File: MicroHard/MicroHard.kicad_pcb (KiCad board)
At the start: 4 copper layers, 222 x 144.5 mm, 206 parts, among them IC1 IS66WVO32M8DBLL-166BLI, J1 USB_B_Micro, J2 Micro_SD_Card_Det2, J3 GPIO_header, J4 MCU_Debug, J5 Controller Connector, J6 FPGA_GPIO_header, J7 FPGA_DEBUG, J8 L77HDE15SD1CH4FVGA, SW1 KMR221NGLFS, SW2 KMR221NGLFS, SW3 KMR221NGLFS, SW4 KMR221NGLFS, U1 TPS54325, U2 TPS54294, U3 EFM32GG842F1024, U4 XC7A100T-FTG256, U5 MAX6955 Display Driver, U6 SN74ALVC245PWR, U7 SN74ALVC245PWR, U8 MT25QL256ABA8ESF-0SIT, Y1 48MHz, Y2 CB3-3C-20M000000

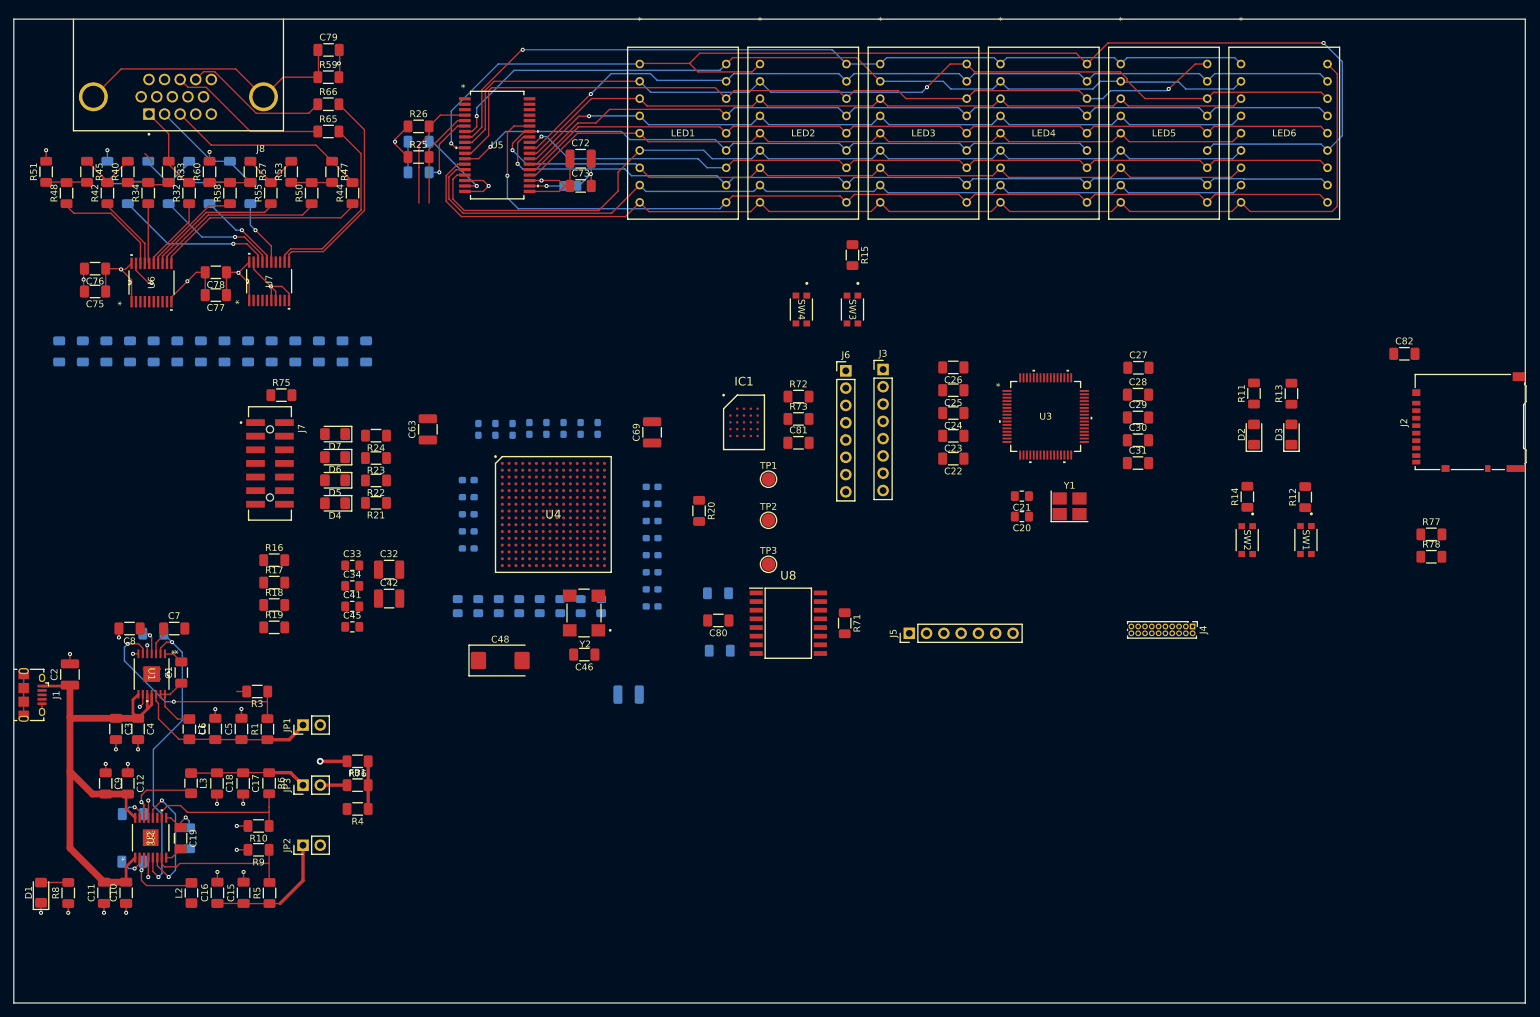
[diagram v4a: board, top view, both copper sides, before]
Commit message: Add MCU
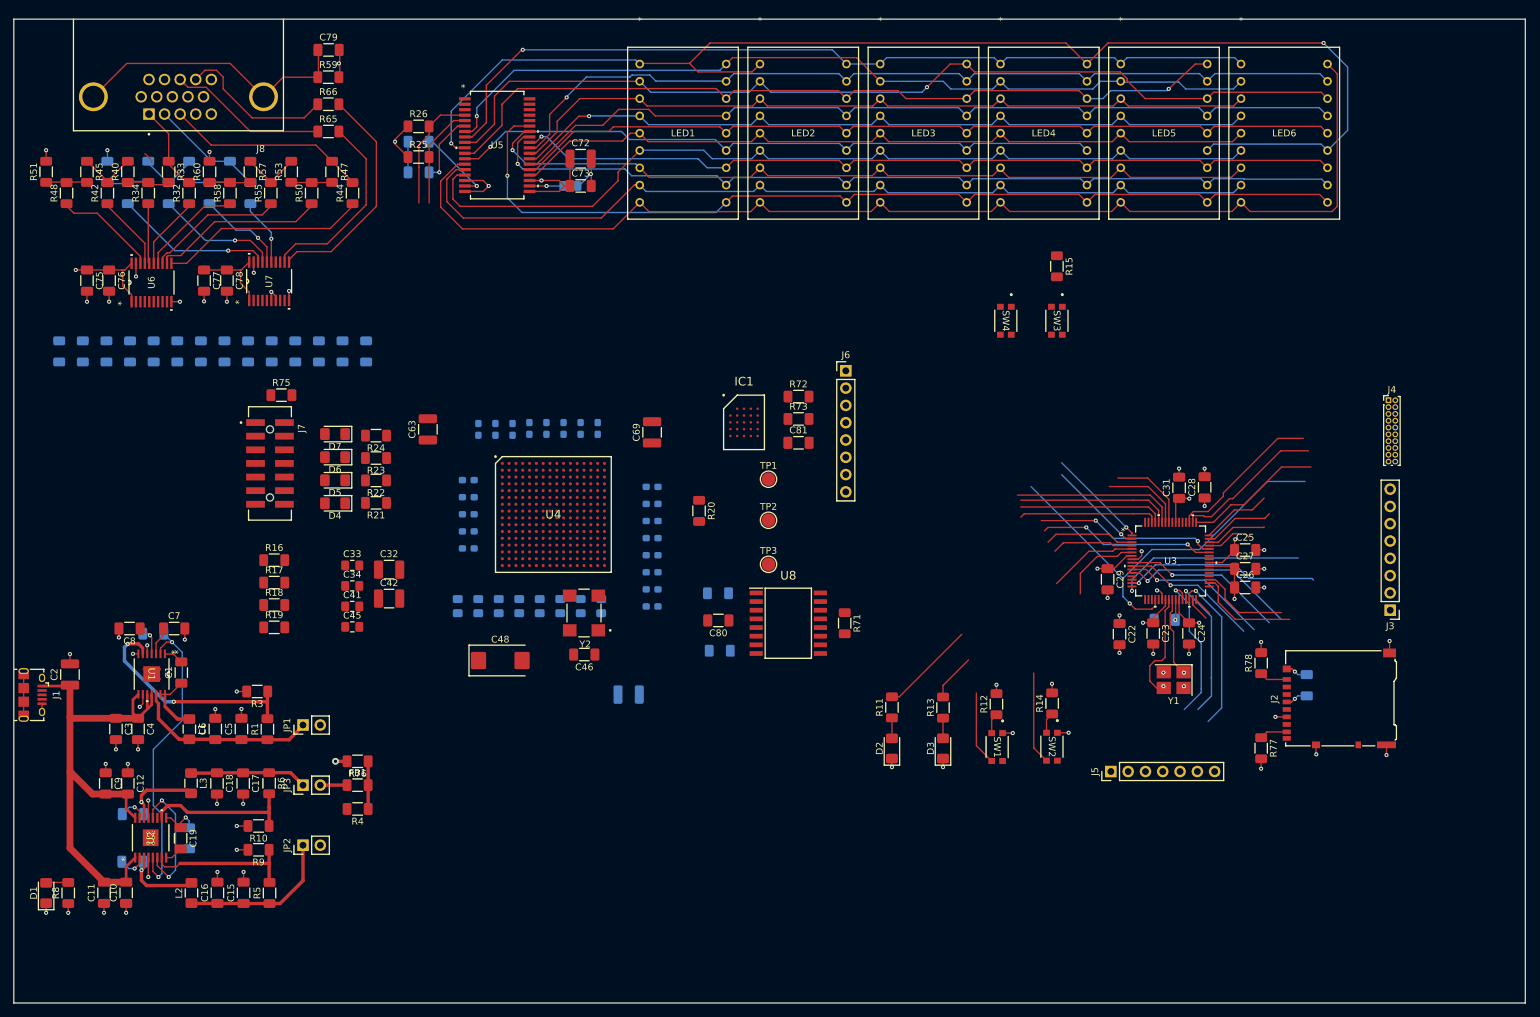
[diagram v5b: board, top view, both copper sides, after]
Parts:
- C20, C21, C30, C82: moved to B.Cu
- moved J3 82.4 mm to (240.2, 115.8), turned to 180 degrees
- moved D2 70.4 mm to (167.0, 136.1)
- moved R11 70.4 mm to (167.0, 130.1)
- moved D3 68.9 mm to (174.5, 136.1)
- moved R13 68.9 mm to (174.5, 130.1)
- moved SW1 54.6 mm to (182.4, 135.9)
- moved R12 54.6 mm to (182.3, 129.6)
- moved C26 53.7 mm to (218.9, 112.5), turned to 0 degrees
- moved C82 50.7 mm to (227.9, 126.8), turned to 90 degrees
- moved C25 48.9 mm to (218.9, 107.0), turned to 0 degrees
- moved C24 47.4 mm to (210.6, 119.2), turned to -90 degrees
- moved J2 44.8 mm to (232.7, 128.8)
- moved J4 43.9 mm to (239.9, 85.0), turned to 0 degrees
- moved SW2 41.8 mm to (190.5, 135.9)
- moved R14 41.8 mm to (190.5, 129.5)
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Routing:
- net MCU_Reset: track 0.00 -> 61.0 mm, vias 0 -> 1
- net +3.3V: track 52.7 -> 97.0 mm, vias 6 -> 18
- net US1_CLK: track 0.00 -> 28.9 mm, vias 0 -> 1
- net US1_CS: track 0.00 -> 28.0 mm, vias 0 -> 1
- net Net-(U3B-PA2): track 0.00 -> 27.3 mm
- net FPGA_RESET: track 0.00 -> 26.6 mm, vias 0 -> 2
- net SD_US2_CS: track 0.00 -> 26.1 mm, vias 0 -> 1
- net FPGA_DONE: track 0.00 -> 25.9 mm, vias 0 -> 2
- net MCU_Btn_2: track 0.00 -> 25.5 mm
- net FPGA_US0_TX: track 0.00 -> 24.2 mm
- net MCU_Btn_1: track 0.00 -> 24.1 mm
- net SD_US2_TX: track 0.00 -> 23.8 mm, vias 0 -> 1
- net Controller_Z: track 0.00 -> 23.6 mm, vias 0 -> 1
- net Net-(J4-Pin_13): track 0.00 -> 22.7 mm
- net FPGA_US0_RX: track 0.00 -> 22.6 mm
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
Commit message: finished memory
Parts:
- removed C58: 470n, Capacitor_SMD:C_0603_1608Metric_Pad1.08x0.95mm_HandSolder
- removed R28, R29, R30, R31, R36, R37, R38, R39, R61, R62, R63, R64, R67, R68: 100k, Resistor_SMD:R_1206_3216Metric_Pad1.30x1.75mm_HandSolder
- C33, C34, C41, C45: moved to B.Cu
- C47, R69, R70: moved to F.Cu
- moved D4 66.8 mm to (148.5, 78.8)
- moved D5 66.8 mm to (148.5, 75.4)
- moved D6 66.8 mm to (148.5, 72.0)
- moved D7 66.8 mm to (148.5, 68.6)
- moved R21 66.8 mm to (154.5, 78.7)
- moved R22 66.8 mm to (154.5, 75.4)
- moved R23 66.8 mm to (154.5, 72.1)
- moved R24 66.8 mm to (154.5, 68.8)
- moved C41 42.8 mm to (125.5, 95.2), turned to -90 degrees
- moved C34 40.6 mm to (126.4, 100.0)
- moved C33 40.1 mm to (127.5, 103.8)
- moved C45 37.0 mm to (123.8, 110.0)
- moved C42 35.9 mm to (117.2, 87.5), turned to 90 degrees
- moved R72 33.0 mm to (121.2, 76.2), turned to 90 degrees
- moved C69 32.2 mm to (102.8, 103.6), turned to 180 degrees
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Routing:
- net GND: track 128.9 -> 226.9 mm, vias 62 -> 131
- net +3.3V: track 97.0 -> 164.6 mm, vias 18 -> 44
- net FPGA_CONFIG_CLOCK: track 0.00 -> 33.4 mm, vias 0 -> 2
- net /FPGA/Unit A/Flash Memory/FLASH_W#: track 0.00 -> 30.8 mm, vias 0 -> 2
- net SRAM_DQ2: track 0.00 -> 28.7 mm, vias 0 -> 2
- net /FPGA/Unit A/Flash Memory/FLASH_HOLD#: track 0.00 -> 26.8 mm
- net +1V0: track 0.00 -> 26.5 mm, vias 0 -> 17
- net SRAM_RESET#: track 0.00 -> 26.2 mm, vias 0 -> 2
- net SRAM_CS#: track 0.00 -> 24.6 mm, vias 0 -> 2
- net /FPGA/Unit A/Flash Memory/FLASH_CS#: track 0.00 -> 22.7 mm, vias 0 -> 2
- net SRAM_DQSM: track 0.00 -> 20.3 mm, vias 0 -> 2
- net SRAM_SCLK: track 0.00 -> 19.8 mm, vias 0 -> 2
- net SRAM_DQ1: track 0.00 -> 19.6 mm, vias 0 -> 2
- net SRAM_DQ5: track 0.00 -> 19.5 mm, vias 0 -> 2
- net /FPGA/Unit A/Flash Memory/FLASH_DQ1: track 0.00 -> 17.6 mm, vias 0 -> 2
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- added copper zone on In4.Cu, net +1V0
- added copper zone on In3.Cu, net +3.3V
- removed copper zone on In2.Cu, net +1V0
- removed copper zone on In2.Cu, net +3.3V
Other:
- copper layers 4 -> 6

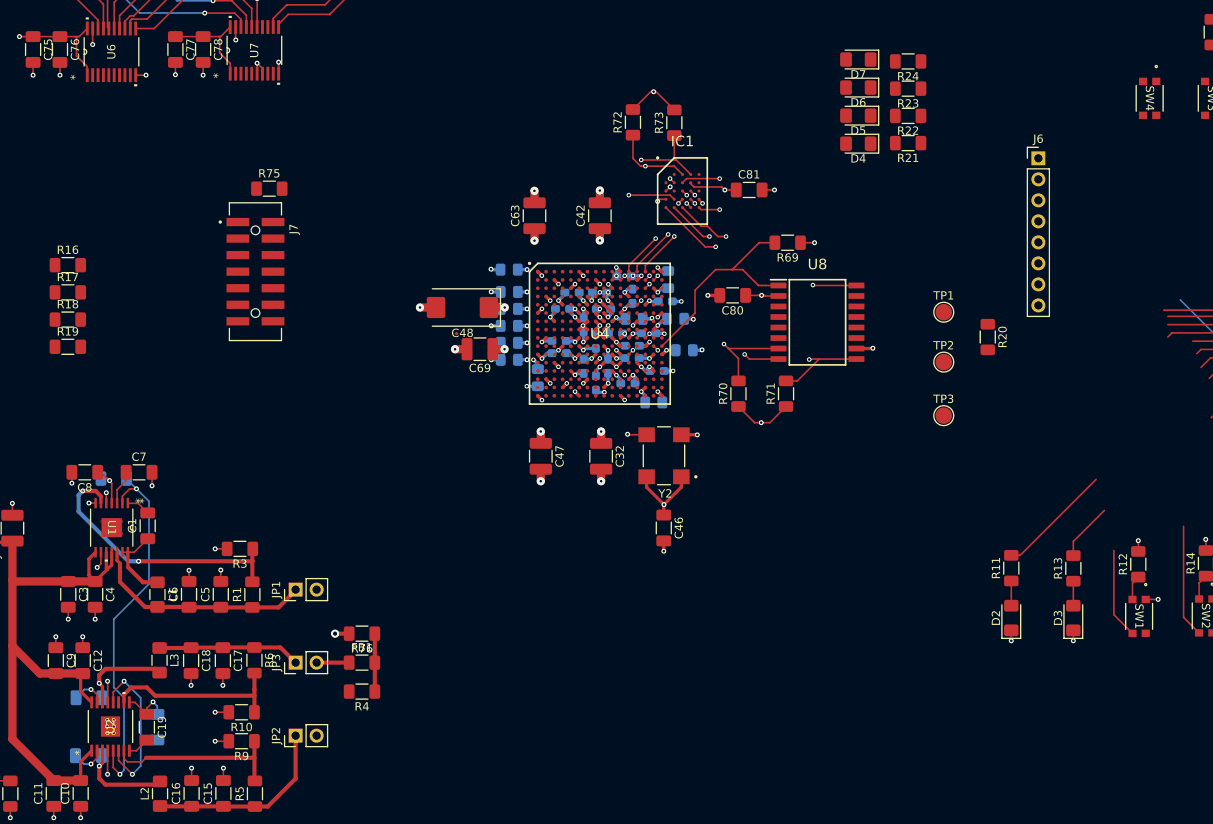
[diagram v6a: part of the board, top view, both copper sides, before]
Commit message: wired up VGA
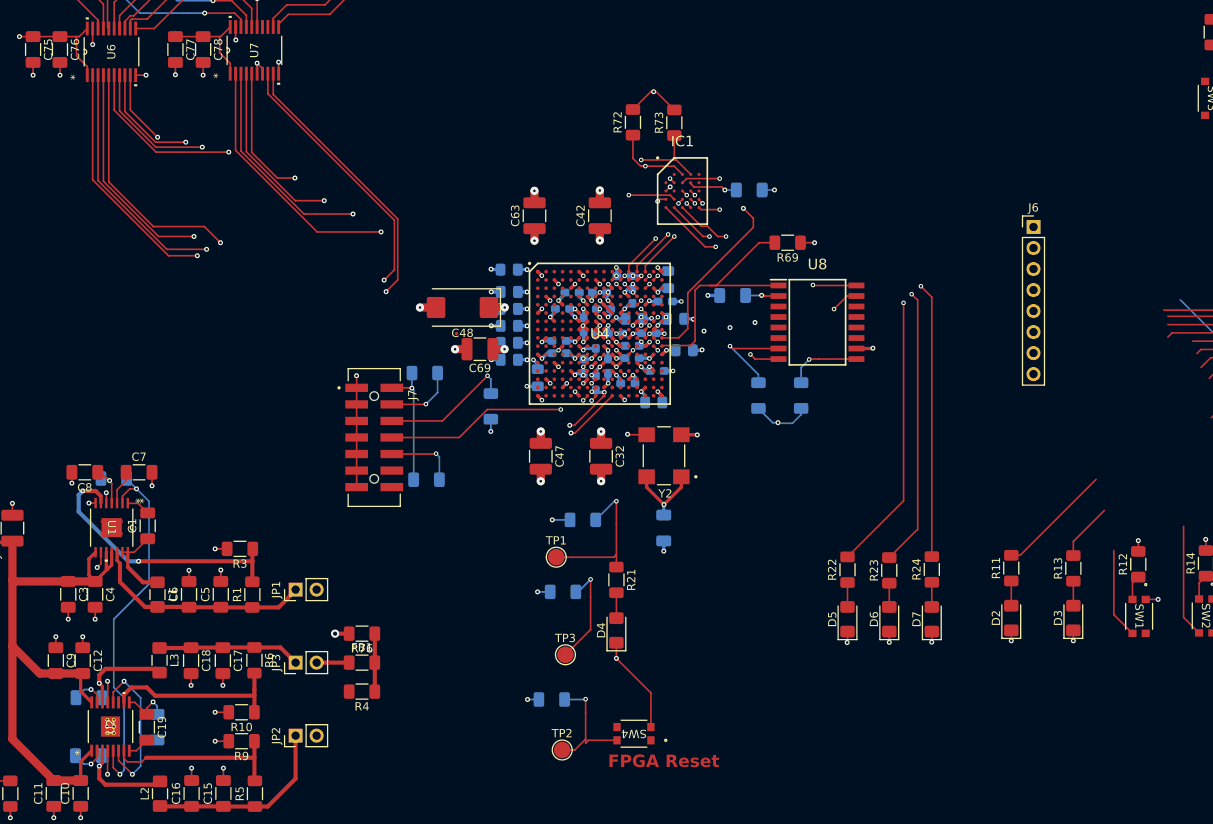
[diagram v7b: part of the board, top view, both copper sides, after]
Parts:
- C46, C80, C81, R16, R17, R18, R19, R20, R70, R71, R75: moved to B.Cu
- moved SW4 98.9 mm to (121.4, 150.1), turned to 180 degrees
- moved R17 69.9 mm to (112.8, 132.9)
- moved R16 69.4 mm to (115.2, 124.2)
- moved R20 68.5 mm to (111.4, 146.0), turned to 180 degrees
- moved D7 68.2 mm to (157.4, 136.3), turned to 90 degrees
- moved TP2 65.8 mm to (112.7, 152.1)
- moved D4 65.7 mm to (119.2, 137.6), turned to 90 degrees
- moved D6 64.4 mm to (152.2, 136.3), turned to 90 degrees
- moved R21 63.5 mm to (119.2, 131.5), turned to -90 degrees
- moved R24 61.5 mm to (157.4, 130.2), turned to 90 degrees
- moved D5 60.9 mm to (147.2, 136.3), turned to 90 degrees
- moved R23 58.3 mm to (152.2, 130.3), turned to 90 degrees
- moved TP1 55.4 mm to (112.0, 128.8)
- moved R22 55.3 mm to (147.2, 130.3), turned to 90 degrees
- moved TP3 54.1 mm to (113.1, 140.6)
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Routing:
- net VGA_B3: track 0.00 -> 113.2 mm, vias 0 -> 3
- net VGA_B2: track 0.00 -> 111.1 mm, vias 0 -> 3
- net VGA_B0: track 0.00 -> 107.2 mm, vias 0 -> 3
- net VGA_B1: track 0.00 -> 106.4 mm, vias 0 -> 2
- net VGA_R2: track 0.00 -> 90.3 mm, vias 0 -> 2
- net VGA_R3: track 0.00 -> 82.6 mm, vias 0 -> 2
- net VGA_R1: track 0.00 -> 82.3 mm, vias 0 -> 2
- net VGA_R0: track 0.00 -> 82.1 mm, vias 0 -> 2
- net VGA_VSYNC: track 0.00 -> 69.9 mm, vias 0 -> 2
- net FPGA_LED2: track 0.00 -> 69.0 mm, vias 0 -> 2
- net FPGA_LED1: track 0.00 -> 68.4 mm, vias 0 -> 2
- net FPGA_LED0: track 0.00 -> 68.2 mm, vias 0 -> 2
- net VGA_G0: track 0.00 -> 67.6 mm, vias 0 -> 2
- net VGA_HSYNC: track 0.00 -> 67.5 mm, vias 0 -> 2
- net VGA_G1: track 0.00 -> 65.7 mm, vias 0 -> 2
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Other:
- board text added: "FPGA Reset"
